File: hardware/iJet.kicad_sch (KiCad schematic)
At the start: 16 parts, among them J1 GPIO, Q3 BSS138, Q4 BSS138, U1 CAT24C256

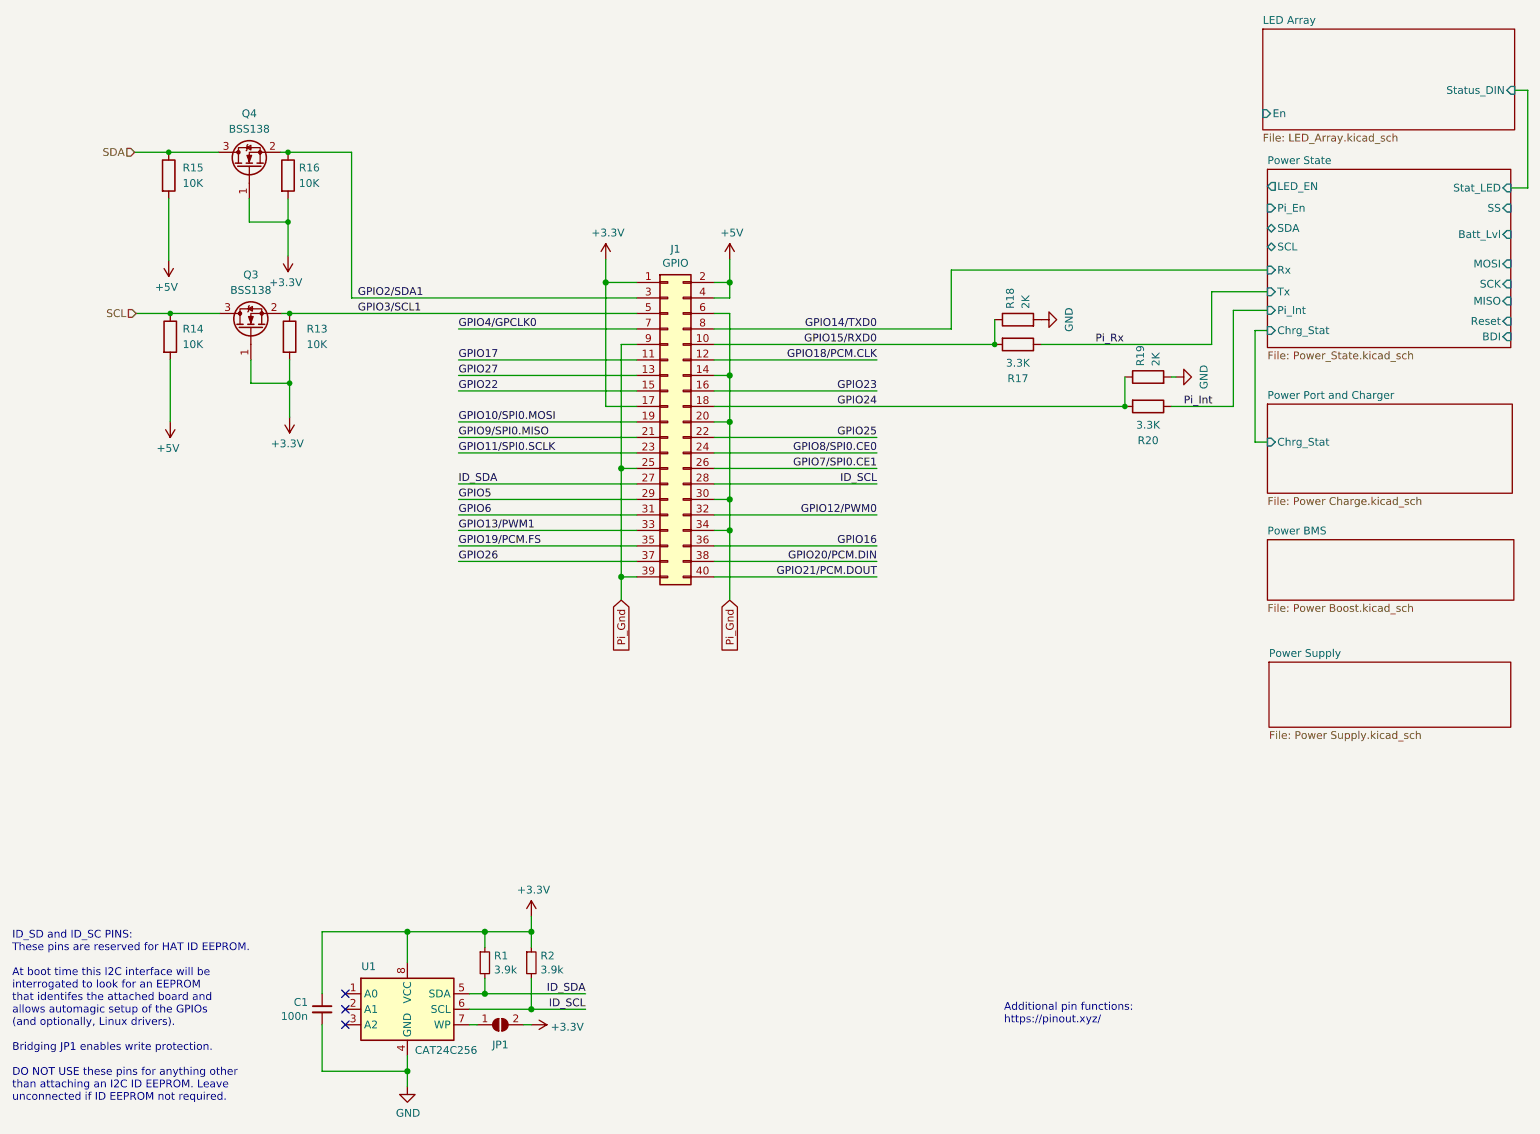
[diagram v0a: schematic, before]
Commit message: Hardware V0.2 - Schematics update
Combines Cell holder, BMS, and voltage regulator into single board
complete w. extensive electrical and thermal protections including:

* MM3220 BMS w Overvoltage, Overcurrent, undervoltage charging/discharge protect
* Fuses on cells, 12v in, 5v and 8.4v out.
* Reverse polarity protection on 12v and cells.

Adds debug UART header
Single IO header on every board
Minor component size corrections
Add current limiting resistor to RPI power NMOS gate.
Add optional support for MLCC/tantalum caps for Voltage Regulator instead of electrolytic
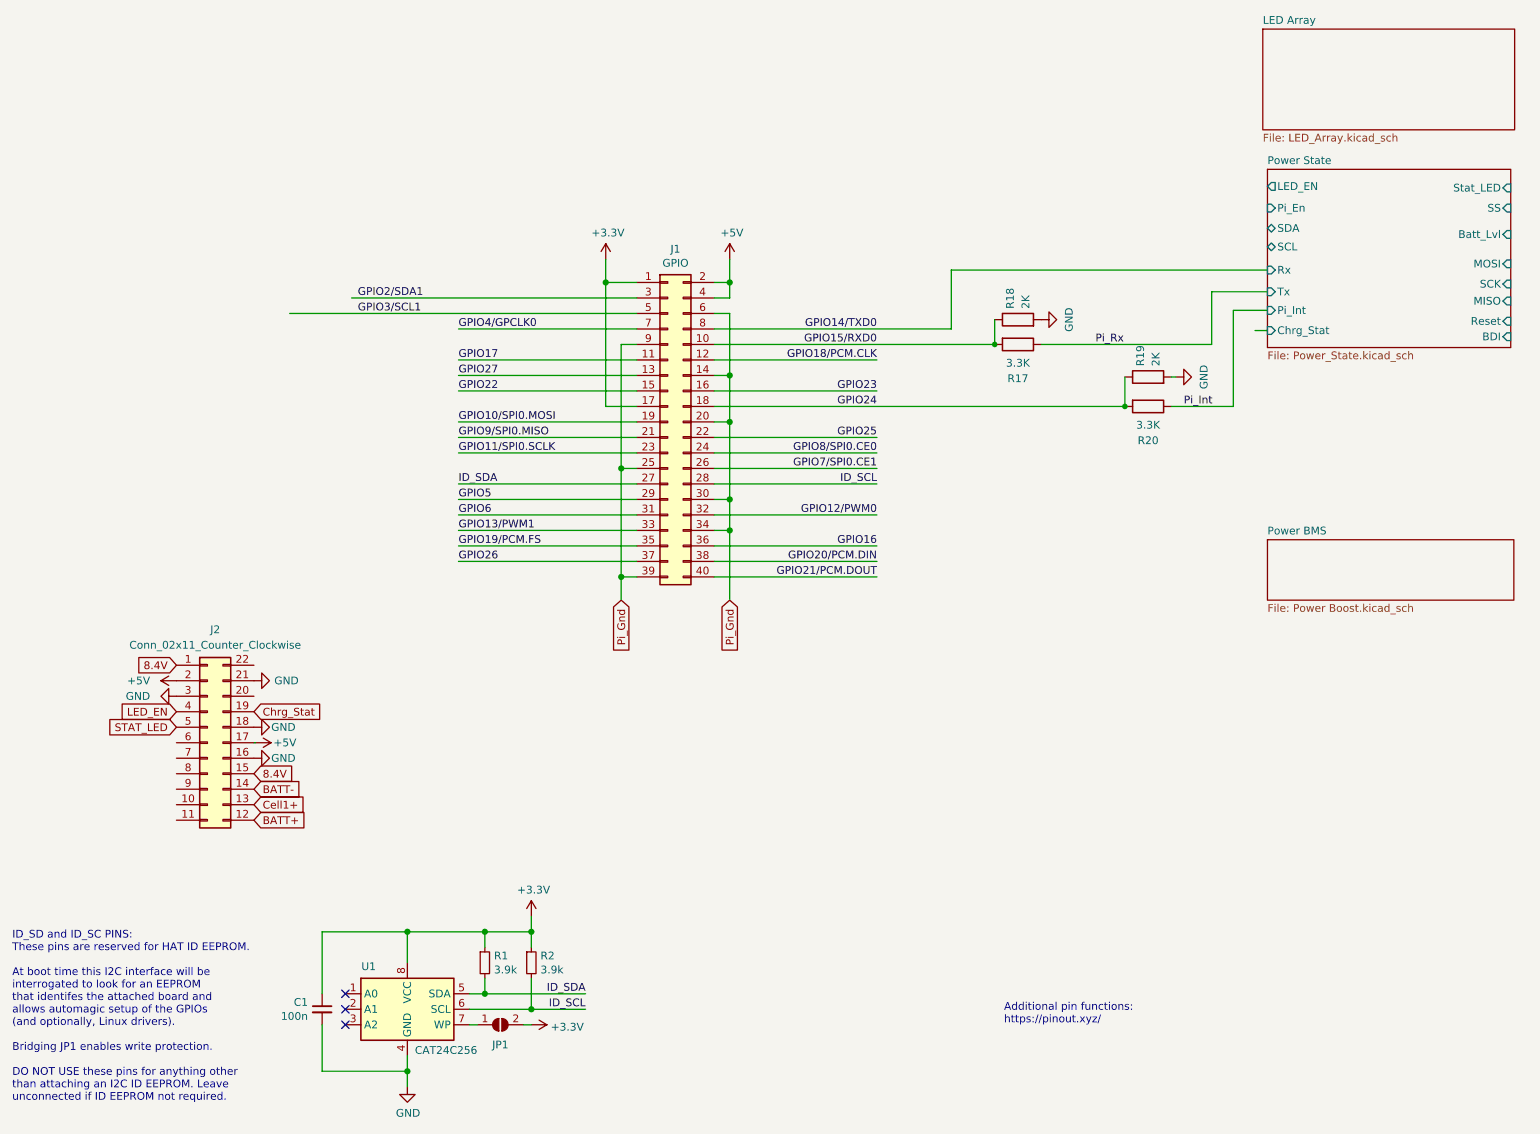
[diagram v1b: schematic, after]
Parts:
- removed Q3, Q4: BSS138, Package_TO_SOT_SMD:SOT-23, symbol Transistor_FET:BSS138
- removed R13, R14, R15, R16: 10K, Resistor_SMD:R_0603_1608Metric_Pad0.98x0.95mm_HandSolder, symbol Device:R
- added J2: Conn_02x11_Counter_Clockwise, Connector_PinSocket_2.54mm:PinSocket_2x11_P2.54mm_Vertical, symbol Connector_Generic:Conn_02x11_Counter_Clockwise
- C1: footprint Resistor_SMD:R_0603_1608Metric_Pad0.98x0.95mm_HandSolder -> Capacitor_SMD:C_0603_1608Metric_Pad1.08x0.95mm_HandSolder
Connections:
- net +5V: now also J2.17 (Pin_17), J2.2 (Pin_2)
- net GND: now also J2.16 (Pin_16), J2.18 (Pin_18), J2.21 (Pin_21), J2.3 (Pin_3)
- new net 8.4V: J2.1 (Pin_1), J2.15 (Pin_15)
- new net BATT+: J2.12 (Pin_12)
- new net BATT-: J2.14 (Pin_14)
- new net Cell1+: J2.13 (Pin_13)
- new net Chrg_Stat: J2.19 (Pin_19)
- new net LED_EN: J2.4 (Pin_4)
- new net STAT_LED: J2.5 (Pin_5)
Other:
- removed sheet Power Port and Charger
- removed sheet Power Supply
- sheet LED Array ports: added none; removed En, Status_DIN
